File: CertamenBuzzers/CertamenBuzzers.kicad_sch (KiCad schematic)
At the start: 57 parts, among them J1 USB_C_Receptacle_USB2.0_14P, J10 RJ45, J11 RJ45, J12 RJ45, J13 RJ45, J2 RJ45, J3 RJ45, J4 RJ45, J5 RJ45, J6 RJ45, J7 RJ45, J8 RJ45, J9 RJ45, SW1 RST, SW10 B4, SW11 C1, SW12 C2, SW13 C3, SW14 C4, SW2 BOOT, SW3 A1, SW4 A2, SW5 A3, SW6 A4, SW7 B1, SW8 B2, SW9 B3, U1 ESP32-S3-WROOM-1, U2 NCP1117-3.3_SOT223, U3 TVS1400DRV

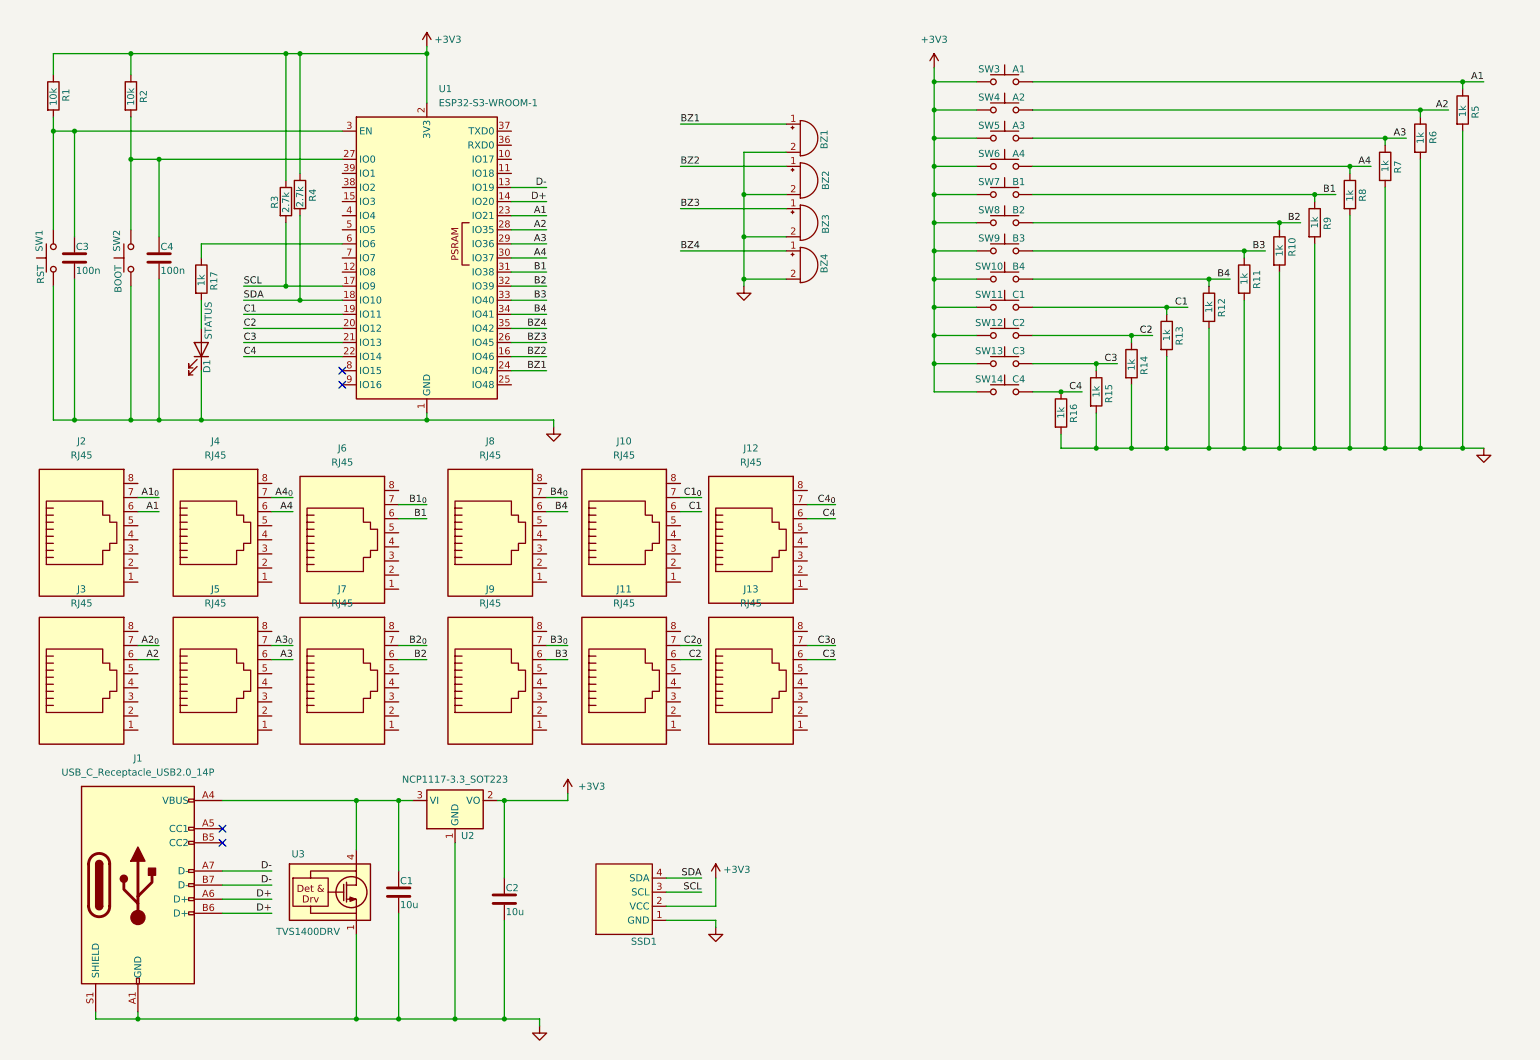
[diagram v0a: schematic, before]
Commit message: Schematic completed
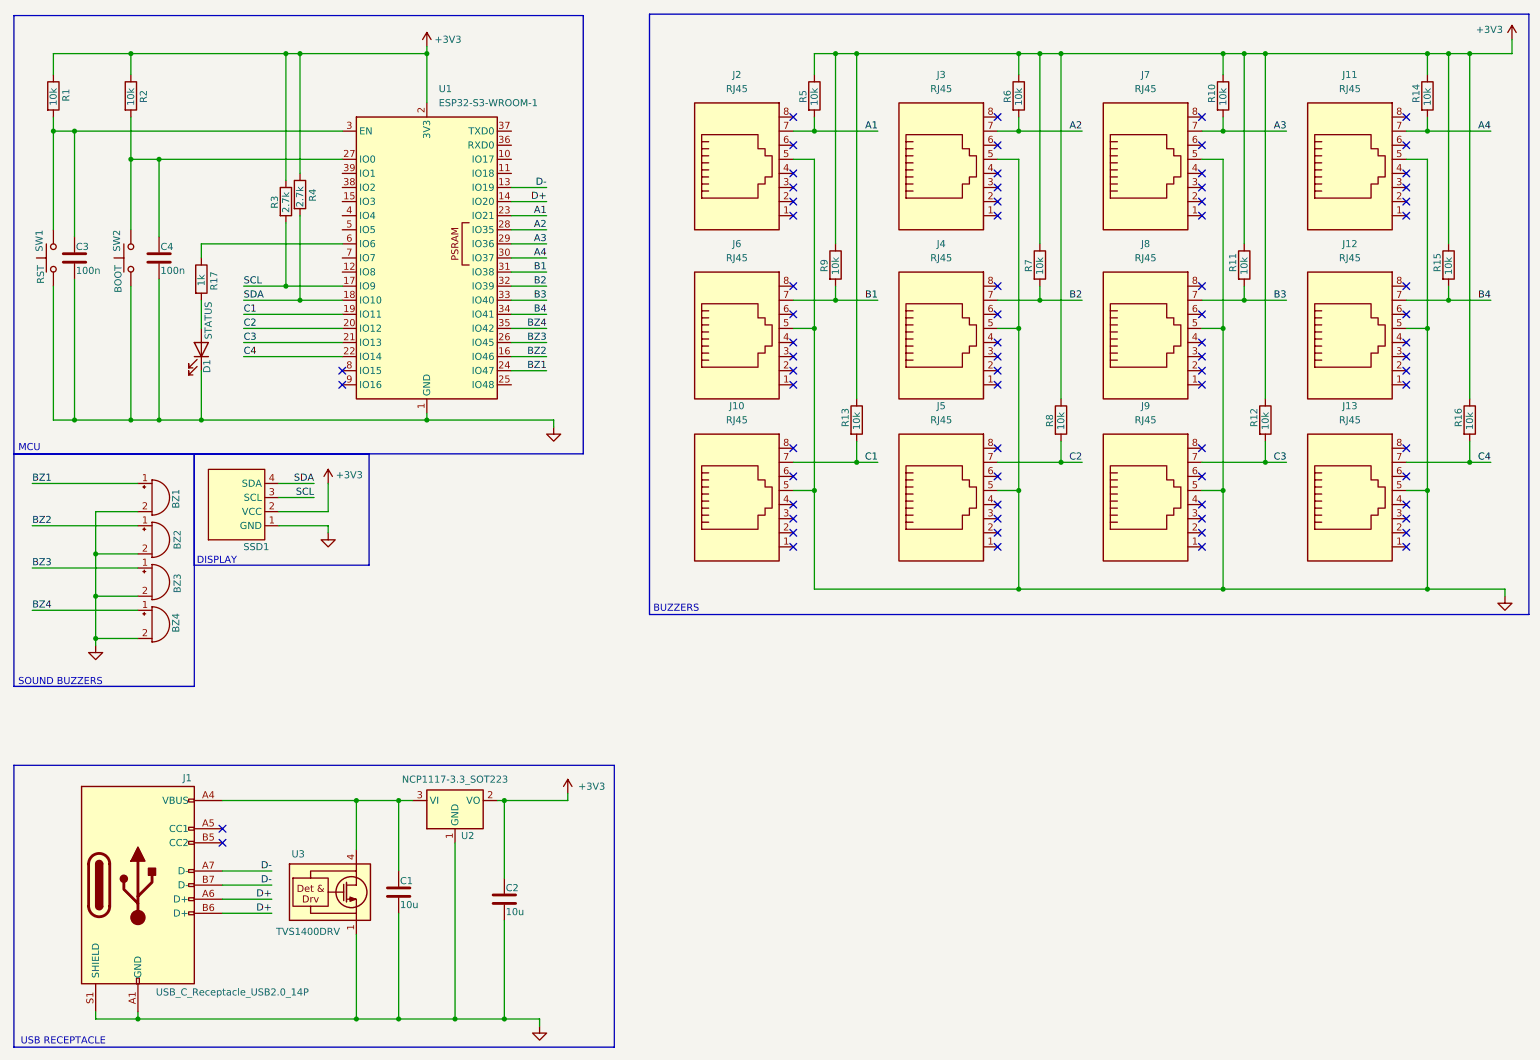
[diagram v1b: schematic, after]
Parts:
- removed SW10: B4, symbol Switch:SW_Push
- removed SW11: C1, symbol Switch:SW_Push
- removed SW12: C2, symbol Switch:SW_Push
- removed SW13: C3, symbol Switch:SW_Push
- removed SW14: C4, symbol Switch:SW_Push
- removed SW3: A1, symbol Switch:SW_Push
- removed SW4: A2, symbol Switch:SW_Push
- removed SW5: A3, symbol Switch:SW_Push
- removed SW6: A4, symbol Switch:SW_Push
- removed SW7: B1, symbol Switch:SW_Push
- removed SW8: B2, symbol Switch:SW_Push
- removed SW9: B3, symbol Switch:SW_Push
- R10, R11, R12, R13, R14, R15, R16, R5, R6, R7, R8, R9: value 1k -> 10k
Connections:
- net A1_{0} is gone; now on net A1: J2.7
- net A2_{0} is gone; now on net A2: J3.7
- net A3_{0} is gone; now on net C2: J5.7
- net A4_{0} is gone; now on net B2: J4.7
- net B1_{0} is gone; now on net B1: J6.7
- net B2_{0} is gone; now on net A3: J7.7
- net B3_{0} is gone; now on net C3: J9.7
- net B4_{0} is gone; now on net B3: J8.7
- net C1_{0} is gone; now on net C1: J10.7
- net C2_{0} is gone; now on net A4: J11.7
- net C3_{0} is gone; now on net C4: J13.7
- net C4_{0} is gone; now on net B4: J12.7
- net +3V3: now also R10.1, R11.1, R12.1, R13.1, R14.1, R15.1, R16.1, R5.1, R6.1, R7.1, R8.1, R9.1
- net A1: now also R5.2; no longer J2.6, R5.1
- net A2: now also R6.2; no longer J3.6, R6.1
- net A3: now also R10.2; no longer J5.6, R7.1
- net A4: now also R14.2; no longer J4.6, R8.1
- net B1: now also R9.2; no longer J6.6, R9.1
- net B2: now also R7.2; no longer J7.6, R10.1
- net B3: now also R11.2; no longer J9.6, R11.1
- net B4: now also R15.2; no longer J8.6, R12.1
- net C1: now also R13.2; no longer J10.6, R13.1
- net C2: now also R8.2; no longer J11.6, R14.1
- net C3: now also R12.2; no longer J13.6, R15.1
- net C4: now also R16.2; no longer J12.6, R16.1
- net GND: now also J10.5, J11.5, J12.5, J13.5, J2.5, J3.5, J4.5, J5.5, J6.5, J7.5, J8.5, J9.5; no longer R10.2, R11.2, R12.2, R13.2, R14.2, R15.2, R16.2, R5.2, R6.2, R7.2, R8.2, R9.2
- no-connect marks 4 -> 76
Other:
- note added: "BUZZERS"
- note added: "DISPLAY"
- note added: "MCU"
- note added: "SOUND BUZZERS"
- note added: "USB RECEPTACLE"
- moved on the sheet: BZ1, BZ2, BZ3, BZ4, SSD1

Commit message: schematic cost optimized
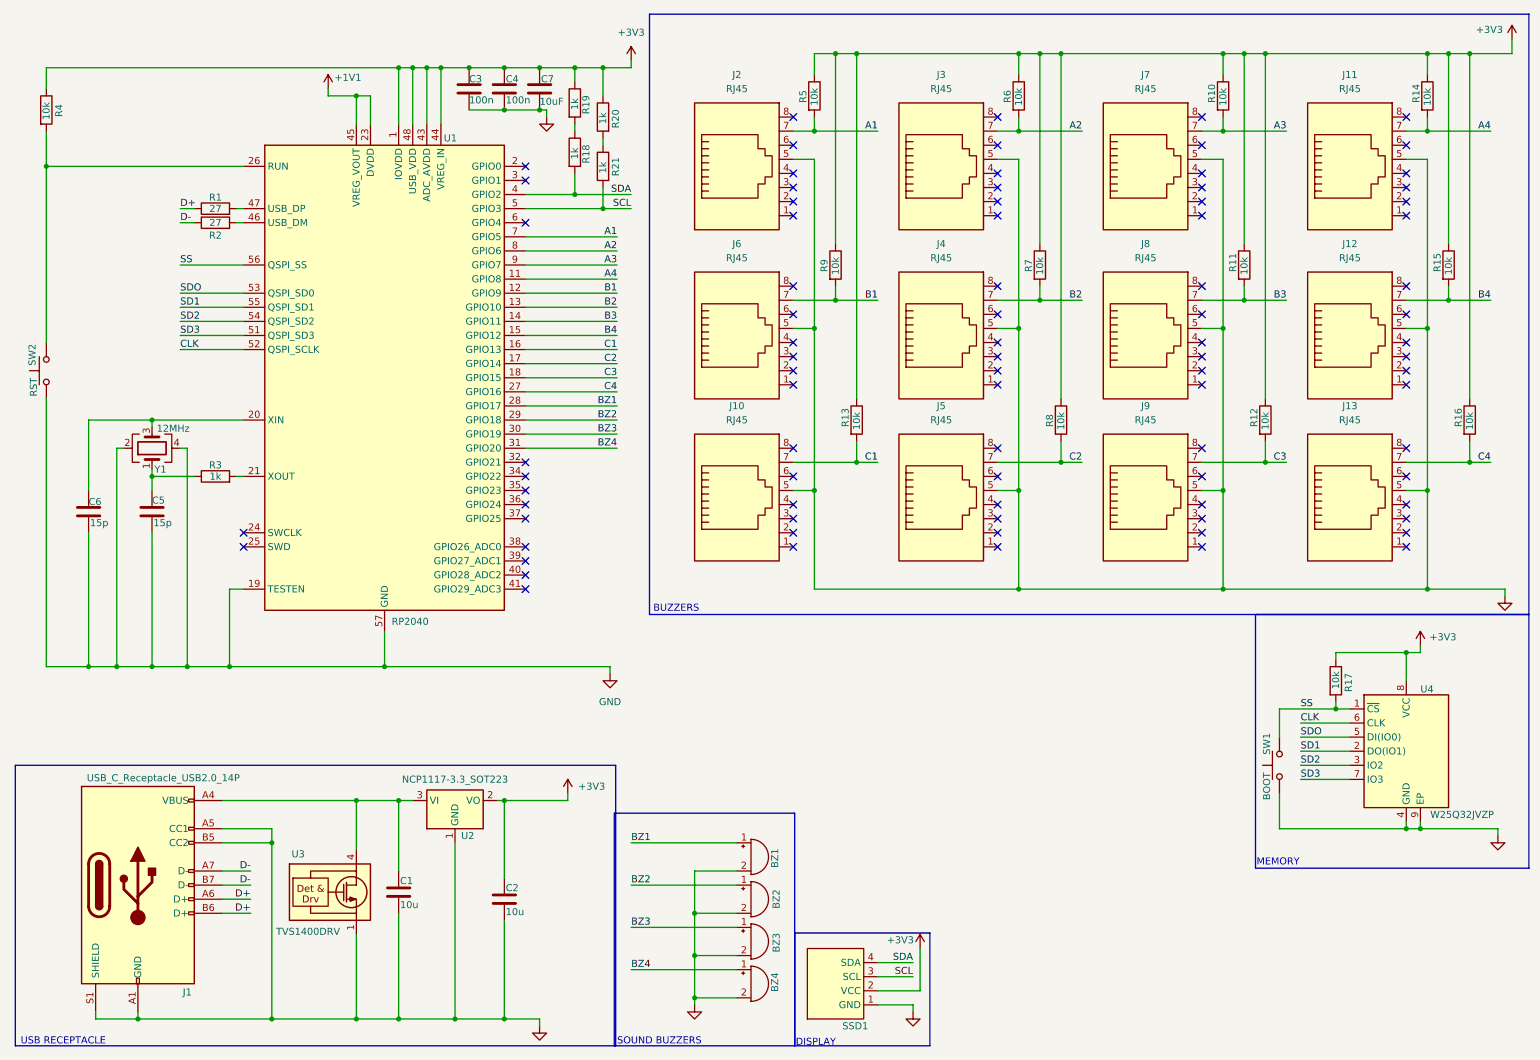
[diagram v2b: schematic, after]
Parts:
- removed D1: STATUS, symbol Device:LED
- removed U1: ESP32-S3-WROOM-1, RF_Module:ESP32-S3-WROOM-1, symbol RF_Module:ESP32-S3-WROOM-1
- added C5, C6: 15p, Capacitor_SMD:C_0603_1608Metric, symbol Device:C
- added C7: 10uF, Capacitor_SMD:C_0805_2012Metric, symbol Device:C
- added R18, R19, R20, R21: 1k, Resistor_SMD:R_0603_1608Metric, symbol Device:R
- added U1: RP2040, Package_DFN_QFN:QFN-56-1EP_7x7mm_P0.4mm_EP3.2x3.2mm, symbol MCU_RaspberryPi:RP2040
- added U4: W25Q32JVZP, Package_SON:WSON-8-1EP_6x5mm_P1.27mm_EP3.4x4.3mm, symbol Memory_Flash:W25Q32JVZP
- added Y1: 12MHz, Crystal:Crystal_SMD_2520-4Pin_2.5x2.0mm, symbol Device:Crystal_GND24
- BZ1, BZ2, BZ3, BZ4: footprint (none) -> Buzzer_Beeper:Buzzer_TDK_PS1240P02BT_D12.2mm_H6.5mm
- C1, C2, C3, C4: footprint (none) -> Capacitor_SMD:C_0805_2012Metric
- J1: footprint (none) -> Connector_USB:USB_C_Receptacle_GCT_USB4105-xx-A_16P_TopMnt_Horizontal
- J10, J11, J12, J13, J2, J3, J4, J5, J6, J7, J8, J9: footprint (none) -> Buzzers:ADAMTECH_MTJ-88ARX1-FSM-LG
- R1, R2: value 10k -> 27; footprint (none) -> Resistor_SMD:R_0603_1608Metric
- R10, R11, R12, R13, R14, R15, R16, R5, R6, R7, R8, R9: footprint (none) -> Resistor_SMD:R_0603_1608Metric
- R17: value 1k -> 10k; footprint (none) -> Resistor_SMD:R_0603_1608Metric
- R3: value 2.7k -> 1k; footprint (none) -> Resistor_SMD:R_0603_1608Metric
- R4: value 2.7k -> 10k; footprint (none) -> Resistor_SMD:R_0603_1608Metric
- SSD1: footprint (none) -> Connector_PinSocket_2.54mm:PinSocket_1x04_P2.54mm_Vertical
- SW1: value RST -> BOOT; footprint (none) -> Button_Switch_SMD:SW_Push_1P1T_NO_CK_KMR2
- SW2: value BOOT -> RST; footprint (none) -> Button_Switch_SMD:SW_Push_1P1T_NO_CK_KMR2
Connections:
- net +3V3: now also C3.1, C4.1, R17.1, C7.1, R19.1, R20.1, U1.1 (IOVDD), U1.10 (IOVDD), U1.22 (IOVDD), U1.33 (IOVDD), U1.42 (IOVDD), U1.43 (ADC_AVDD), U1.44 (VREG_IN), U1.48 (USB_VDD), U1.49 (IOVDD), U4.8 (VCC); no longer R1.1, R2.1, R3.1
- net A1: now also U1.7 (GPIO5)
- net A2: now also U1.8 (GPIO6)
- net A3: now also U1.9 (GPIO7)
- net A4: now also U1.11 (GPIO8)
- net B1: now also U1.12 (GPIO9)
- net B2: now also U1.13 (GPIO10)
- net B3: now also U1.14 (GPIO11)
- net B4: now also U1.15 (GPIO12)
- net BZ1: now also U1.28 (GPIO17)
- net BZ2: now also U1.29 (GPIO18)
- net BZ3: now also U1.30 (GPIO19)
- net BZ4: now also U1.31 (GPIO20)
- net C1: now also U1.16 (GPIO13)
- net C2: now also U1.17 (GPIO14)
- net C3: now also U1.18 (GPIO15)
- net C4: now also U1.27 (GPIO16)
- net D+: now also R1.1
- net D-: now also R2.1
- net GND: now also J1.A5 (CC1), J1.B5 (CC2), C5.2, C6.2, C7.2, U1.19 (TESTEN), U1.57 (GND), U4.4 (GND), U4.9 (EP), Y1.2, Y1.4
- net SCL: now also R21.2, U1.5 (GPIO3); no longer R3.2
- net SDA: now also R18.2, U1.4 (GPIO2); no longer R4.2
- net SS: now reaches R17.2
- net SS: now also SW1.2, U1.56 (QSPI_SS), U4.1 (~{CS})
- new net: R18.1, R19.2
- new net: R4.2, SW2.2, U1.26 (RUN)
- new net: R2.2, U1.46 (USB_DM)
- new net: C5.1, R3.1, Y1.1
- new net: C6.1, U1.20 (XIN), Y1.3
- new net: R3.2, U1.21 (XOUT)
- new net: R1.2, U1.47 (USB_DP)
- new net: R20.2, R21.1
- new net +1V1: U1.23 (DVDD), U1.45 (VREG_VOUT), U1.50 (DVDD)
- new net CLK: U1.52 (QSPI_SCLK), U4.6 (CLK)
- new net SD1: U1.55 (QSPI_SD1), U4.2 (DO(IO1))
- new net SD2: U1.54 (QSPI_SD2), U4.3 (IO2)
- new net SD3: U1.51 (QSPI_SD3), U4.7 (IO3)
- new net SDO: U1.53 (QSPI_SD0), U4.5 (DI(IO0))
- no-connect marks 76 -> 86
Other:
- note added: "MEMORY"
- note removed: "MCU"
- moved on the sheet: BZ1, BZ2, BZ3, BZ4, SSD1

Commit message: scheamtic done + cost optimized some more
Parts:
- removed J10, J11, J12, J13, J2, J3, J4, J5, J6, J7, J8, J9: RJ45, Buzzers:ADAMTECH_MTJ-88ARX1-FSM-LG, symbol Connector:RJ45
- added J10, J11, J12, J14, J2, J3, J4, J5, J6, J7, J8, J9: RJ12, Buzzers:ADAMTECH_MTJ-88ARX1-FSM-LG, symbol Connector:RJ12
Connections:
- net A1: now also J3.5
- net A2: now also J6.5
- net A3: now also J7.5
- net A4: now also J12.5
- net B1: now also J2.5
- net B2: now also J5.5
- net B3: now also J8.5
- net B4: now also J11.5
- net C1: now also J14.5
- net C2: now also J4.5
- net C3: now also J9.5
- net C4: now also J10.5
- net GND: now also J10.3, J11.3, J12.3, J14.3, J2.3, J3.3, J4.3, J5.3, J6.3, J7.3, J8.3, J9.3
- no-connect marks 86 -> 62

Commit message: pcb done
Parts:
- C7: value 10uF -> 10u
- J10: value RJ12 -> C4
- J11: value RJ12 -> B4
- J12: value RJ12 -> A4
- J14: value RJ12 -> C1
- J2: value RJ12 -> B1
- J3: value RJ12 -> A1
- J4: value RJ12 -> C2
- J5: value RJ12 -> B2
- J6: value RJ12 -> A2
- J7: value RJ12 -> A3
- J8: value RJ12 -> B3
- J9: value RJ12 -> C3
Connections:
- net +5V: now reaches C1.1, J1.A4 (VBUS), J1.A9 (VBUS), J1.B4 (VBUS), J1.B9 (VBUS), U2.3 (VI), U3.4 (IN), U3.5 (IN), U3.6 (IN)
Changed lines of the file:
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@@
 	)
 	(junction
+		(at 63.5 153.67)
+		(diameter 0)
+		(color 0 0 0 0)
+	)
+	(junction
 		(at 100.33 153.67)
 		(diameter 0)
@@
 	(wire
 		(pts
+			(xy 63.5 152.4) (xy 63.5 153.67)
+		)
+		(stroke
+			(width 0)
+			(type default)
+		)
+	)
+	(wire
+		(pts
 			(xy 226.06 68.58) (xy 229.87 68.58)
 		)
@@
 	(wire
 		(pts
-			(xy 49.53 153.67) (xy 73.66 153.67)
+			(xy 49.53 153.67) (xy 63.5 153.67)
 		)
 		(stroke
@@
 	(wire
 		(pts
+			(xy 63.5 153.67) (xy 73.66 153.67)
+		)
+		(stroke
+			(width 0)
+			(type default)
+		)
+	)
+	(wire
+		(pts
 			(xy 106.68 21.59) (xy 113.03 21.59)
 		)
@@
 			)
 		)
-		(property "Value" "RJ12"
+		(property "Value" "B2"
 			(at 179.07 55.88 0)
 			(effects
@@
 			)
 		)
-		(property "Value" "RJ12"
+		(property "Value" "A1"
 			(at 142.24 25.4 0)
 			(effects
@@
 			)
 		)
-		(property "Value" "10uF"
+		(property "Value" "10u"
 			(at 106.68 27.686 0)
 			(effects
@@
 			)
 		)
-		(property "Value" "RJ12"
+		(property "Value" "A4"
 			(at 252.73 25.4 0)
 			(effects
@@
 			)
 		)
-		(property "Value" "RJ12"
+		(property "Value" "B3"
 			(at 215.9 55.88 0)
 			(effects
@@
 	)
 	(symbol
+		(lib_id "power:+5V")
+		(at 63.5 152.4 0)
+		(unit 1)
+		(exclude_from_sim no)
+		(in_bom yes)
+		(on_board yes)
+		(dnp no)
+		(property "Reference" "#PWR014"
+			(at 63.5 156.21 0)
+			(effects
+				(font
+					(size 1.27 1.27)
+				)
+				(hide yes)
+			)
+		)
+		(property "Value" "+5V"
+			(at 66.294 150.368 0)
+			(effects
+				(font
+					(size 1.27 1.27)
+				)
+			)
+		)
+		(property "Footprint" ""
+			(at 63.5 152.4 0)
+			(effects
+				(font
+					(size 1.27 1.27)
+				)
+				(hide yes)
+			)
+		)
+		(property "Datasheet" ""
+			(at 63.5 152.4 0)
+			(effects
+				(font
+					(size 1.27 1.27)
+				)
+				(hide yes)
+			)
+		)
+		(property "Description" "Power symbol creates a global label with name \"+5V\""
+			(at 63.5 152.4 0)
+			(effects
+				(font
+					(size 1.27 1.27)
+				)
+				(hide yes)
+			)
+		)
+		(pin "1"
+		)
+		(instances
+			(project ""
+				(path "/b43f3344-d0bd-486e-a263-136591dff90e"
+					(reference "#PWR014")
+					(unit 1)
+				)
+			)
+		)
+	)
+	(symbol
 		(lib_id "Connector:RJ12")
 		(at 215.9 97.79 0)
@@
 			)
 		)
-		(property "Value" "RJ12"
+		(property "Value" "C3"
 			(at 215.9 85.09 0)
 			(effects
@@
 			)
 		)
-		(property "Value" "RJ12"
+		(property "Value" "B1"
 			(at 142.24 55.88 0)
 			(effects
@@
 			)
 		)
-		(property "Value" "RJ12"
+		(property "Value" "A2"
 			(at 179.07 25.4 0)
 			(effects
@@
 			)
 		)
-		(property "Value" "RJ12"
+		(property "Value" "C2"
 			(at 179.07 85.09 0)
 			(effects
@@
 			)
 		)
-		(property "Value" "RJ12"
+		(property "Value" "A3"
 			(at 215.9 25.4 0)
 			(effects
@@
 			)
 		)
-		(property "Value" "RJ12"
+		(property "Value" "B4"
 			(at 252.73 55.88 0)
 			(effects
@@
 			)
 		)
-		(property "Value" "RJ12"
+		(property "Value" "C1"
 			(at 142.24 85.09 0)
 			(effects
@@
 			)
 		)
-		(property "Value" "RJ12"
+		(property "Value" "C4"
 			(at 252.73 85.09 0)
 			(effects

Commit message: pcb done + receptacles adjusted + 3d models added
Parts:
- added C8: 10u, Capacitor_SMD:C_0805_2012Metric, symbol Device:C
- added C9: 100n, Capacitor_SMD:C_0805_2012Metric, symbol Device:C
- added R22, R23, R24: 10k, Resistor_SMD:R_0603_1608Metric, symbol Device:R
- added SW3: SW_Push, Connector_PinSocket_2.54mm:PinSocket_1x02_P2.54mm_Vertical, symbol Switch:SW_Push
- J10, J11, J12, J14, J2, J3, J4, J5, J6, J7, J8, J9: footprint Buzzers:ADAMTECH_MTJ-88ARX1-FSM-LG -> Connector_RJ:RJ25_Wayconn_MJEA-660X1_Horizontal
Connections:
- net +1V1: now also C8.1, C9.1
- net +3V3: now also R23.1
- net B3: now also U1.15 (GPIO12); no longer U1.14 (GPIO11)
- net B4: now also U1.14 (GPIO11); no longer U1.15 (GPIO12)
- net GND: now also C8.2, C9.2, R22.2, R24.2, SW3.2; no longer J1.A5 (CC1), J1.B5 (CC2)
- net at U1.6 (GPIO4): now also R23.2, SW3.1
- new net: J1.B5 (CC2), R22.1
- new net: J1.A5 (CC1), R24.1
- no-connect marks 62 -> 61

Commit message: buzzer buttons
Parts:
- added R25, R26, R27: 10k, Resistor_SMD:R_0603_1608Metric, symbol Device:R
- added SW4, SW5, SW6: Score_{A}, Connector_PinSocket_2.54mm:PinSocket_1x02_P2.54mm_Vertical, symbol Switch:SW_Push
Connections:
- net +3V3: now also R25.1, R26.1, R27.1
- net GND: now also SW4.1, SW5.1, SW6.1
- net Sc_{B}: now reaches U1.2 (GPIO0)
- net Sc_{B}: now also R26.2, SW5.2
- net Sc_{A}: now reaches U1.3 (GPIO1)
- net Sc_{A}: now also R25.2, SW4.2
- net Sc_{C}: now reaches U1.40 (GPIO28_ADC2)
- net Sc_{C}: now also R27.2, SW6.2
- no-connect marks 61 -> 58
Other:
- moved on the sheet: SW3

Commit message: code button stuff
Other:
- note added: "SCOREBOARD BUTTONS"
- moved on the sheet: C1, C2, R25, R26, R27, SW4, SW5, SW6, U2, U3
